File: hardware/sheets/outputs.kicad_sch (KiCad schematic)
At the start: 52 parts, among them J3 FRONT tail, J4 REAR tail 1 (7-core), J5 REAR tail 2 (7-core), J8 CAN pigtail -> SS1.0 2w, U11 TPS4H160BQPWPRQ1, U12 TPS4H160BQPWPRQ1, U13 TPS4H160BQPWPRQ1

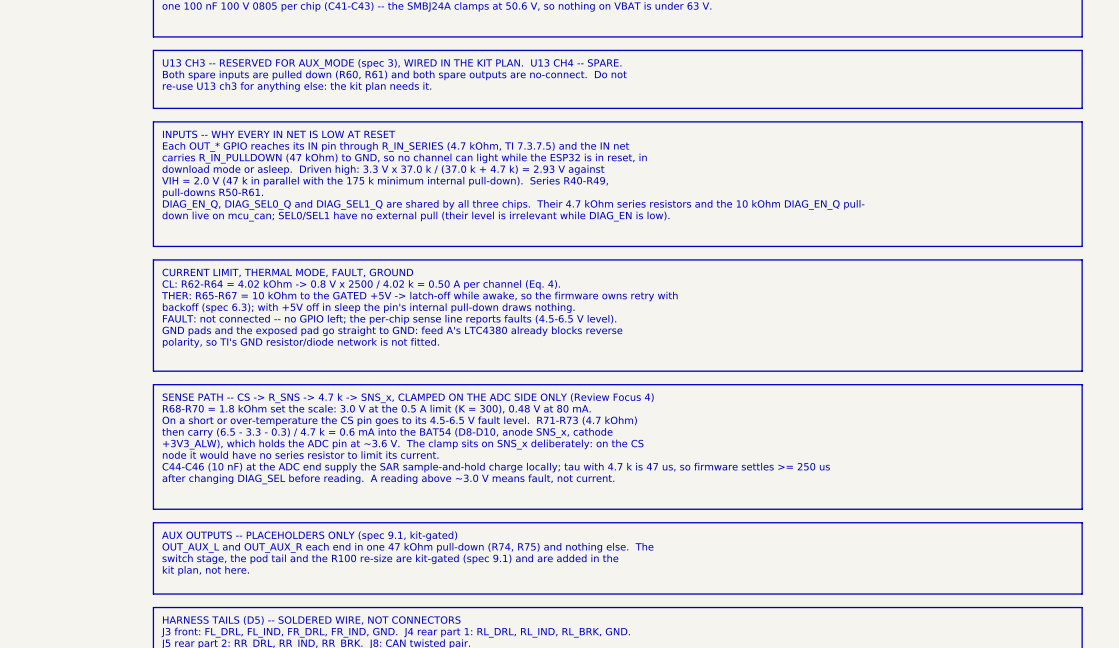
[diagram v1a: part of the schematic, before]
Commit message: fix: final-review wave: DIAG_EN margin, feed-B return before the choke, true protection claims
Co-Authored-By: Claude Opus 5.5 <noreply@anthropic.com>
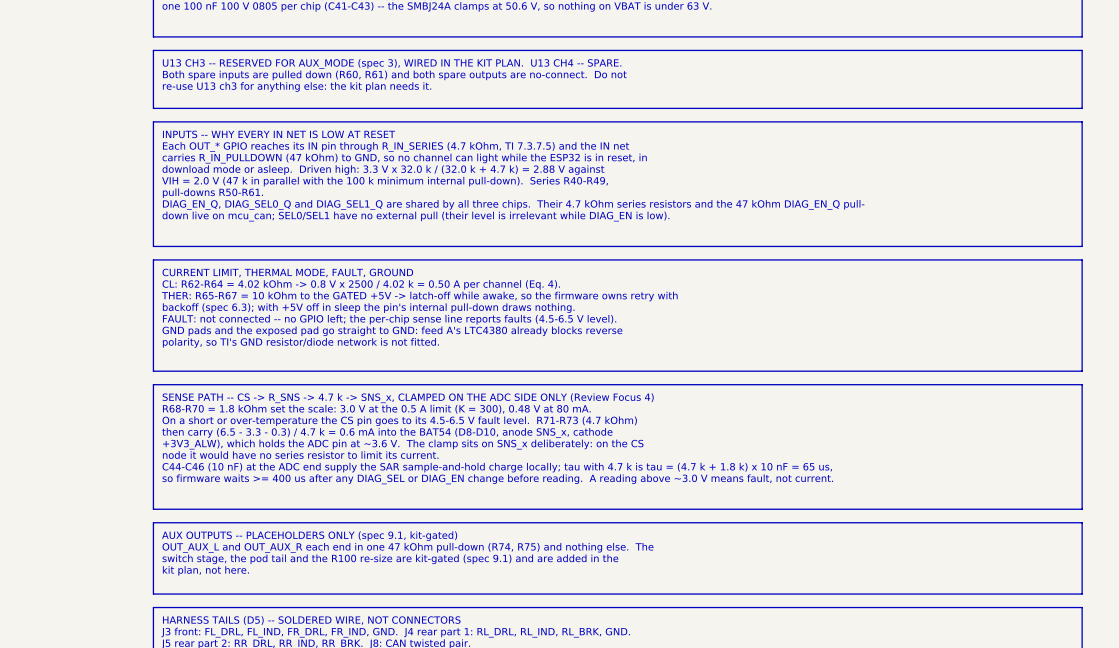
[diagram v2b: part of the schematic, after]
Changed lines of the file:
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@@
 		(title "outputs")
 	)
-	(text_box "SENSE PATH -- CS -> R_SNS -> 4.7 k -> SNS_x, CLAMPED ON THE ADC SIDE ONLY (Review Focus 4)\nR68-R70 = 1.8 kOhm set the scale: 3.0 V at the 0.5 A limit (K = 300), 0.48 V at 80 mA.\nOn a short or over-temperature the CS pin goes to its 4.5-6.5 V fault level.  R71-R73 (4.7 kOhm)\nthen carry (6.5 - 3.3 - 0.3) / 4.7 k = 0.6 mA into the BAT54 (D8-D10, anode SNS_x, cathode\n+3V3_ALW), which holds the ADC pin at ~3.6 V.  The clamp sits on SNS_x deliberately: on the CS\nnode it would have no series resistor to limit its current.\nC44-C46 (10 nF) at the ADC end supply the SAR sample-and-hold charge locally; tau with 4.7 k is 47 us, so firmware settles >= 250 us\nafter changing DIAG_SEL before reading.  A reading above ~3.0 V means fault, not current."
+	(text_box "SENSE PATH -- CS -> R_SNS -> 4.7 k -> SNS_x, CLAMPED ON THE ADC SIDE ONLY (Review Focus 4)\nR68-R70 = 1.8 kOhm set the scale: 3.0 V at the 0.5 A limit (K = 300), 0.48 V at 80 mA.\nOn a short or over-temperature the CS pin goes to its 4.5-6.5 V fault level.  R71-R73 (4.7 kOhm)\nthen carry (6.5 - 3.3 - 0.3) / 4.7 k = 0.6 mA into the BAT54 (D8-D10, anode SNS_x, cathode\n+3V3_ALW), which holds the ADC pin at ~3.6 V.  The clamp sits on SNS_x deliberately: on the CS\nnode it would have no series resistor to limit its current.\nC44-C46 (10 nF) at the ADC end supply the SAR sample-and-hold charge locally; tau with 4.7 k is tau = (4.7 k + 1.8 k) x 10 nF = 65 us,\nso firmware waits >= 400 us after any DIAG_SEL or DIAG_EN change before reading.  A reading above ~3.0 V means fault, not current."
 		(exclude_from_sim no)
 		(at 460.0 65.48 0)
@@
 		)
 	)
-	(text_box "INPUTS -- WHY EVERY IN NET IS LOW AT RESET\nEach OUT_* GPIO reaches its IN pin through R_IN_SERIES (4.7 kOhm, TI 7.3.7.5) and the IN net\ncarries R_IN_PULLDOWN (47 kOhm) to GND, so no channel can light while the ESP32 is in reset, in\ndownload mode or asleep.  Driven high: 3.3 V x 37.0 k / (37.0 k + 4.7 k) = 2.93 V against\nVIH = 2.0 V (47 k in parallel with the 175 k minimum internal pull-down).  Series R40-R49,\npull-downs R50-R61.\nDIAG_EN_Q, DIAG_SEL0_Q and DIAG_SEL1_Q are shared by all three chips.  Their 4.7 kOhm series resistors and the 10 kOhm DIAG_EN_Q pull-\ndown live on mcu_can; SEL0/SEL1 have no external pull (their level is irrelevant while DIAG_EN is low)."
+	(text_box "INPUTS -- WHY EVERY IN NET IS LOW AT RESET\nEach OUT_* GPIO reaches its IN pin through R_IN_SERIES (4.7 kOhm, TI 7.3.7.5) and the IN net\ncarries R_IN_PULLDOWN (47 kOhm) to GND, so no channel can light while the ESP32 is in reset, in\ndownload mode or asleep.  Driven high: 3.3 V x 32.0 k / (32.0 k + 4.7 k) = 2.88 V against\nVIH = 2.0 V (47 k in parallel with the 100 k minimum internal pull-down).  Series R40-R49,\npull-downs R50-R61.\nDIAG_EN_Q, DIAG_SEL0_Q and DIAG_SEL1_Q are shared by all three chips.  Their 4.7 kOhm series resistors and the 47 kOhm DIAG_EN_Q pull-\ndown live on mcu_can; SEL0/SEL1 have no external pull (their level is irrelevant while DIAG_EN is low)."
 		(exclude_from_sim no)
 		(at 460.0 36.28 0)
